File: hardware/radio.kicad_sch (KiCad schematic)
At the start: 22 parts, among them J9 Counterpoise, U6 Si4463

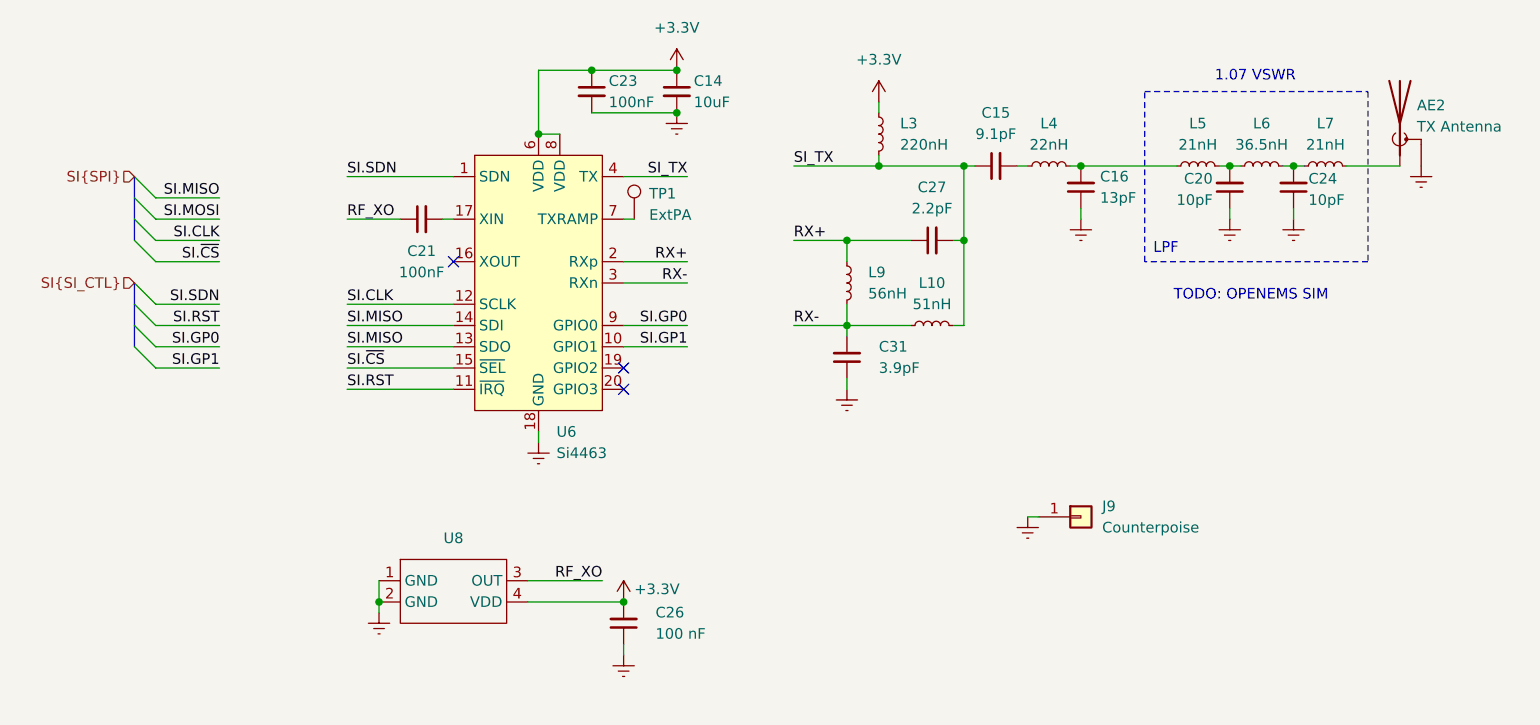
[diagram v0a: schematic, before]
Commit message: power path and bme280 fix
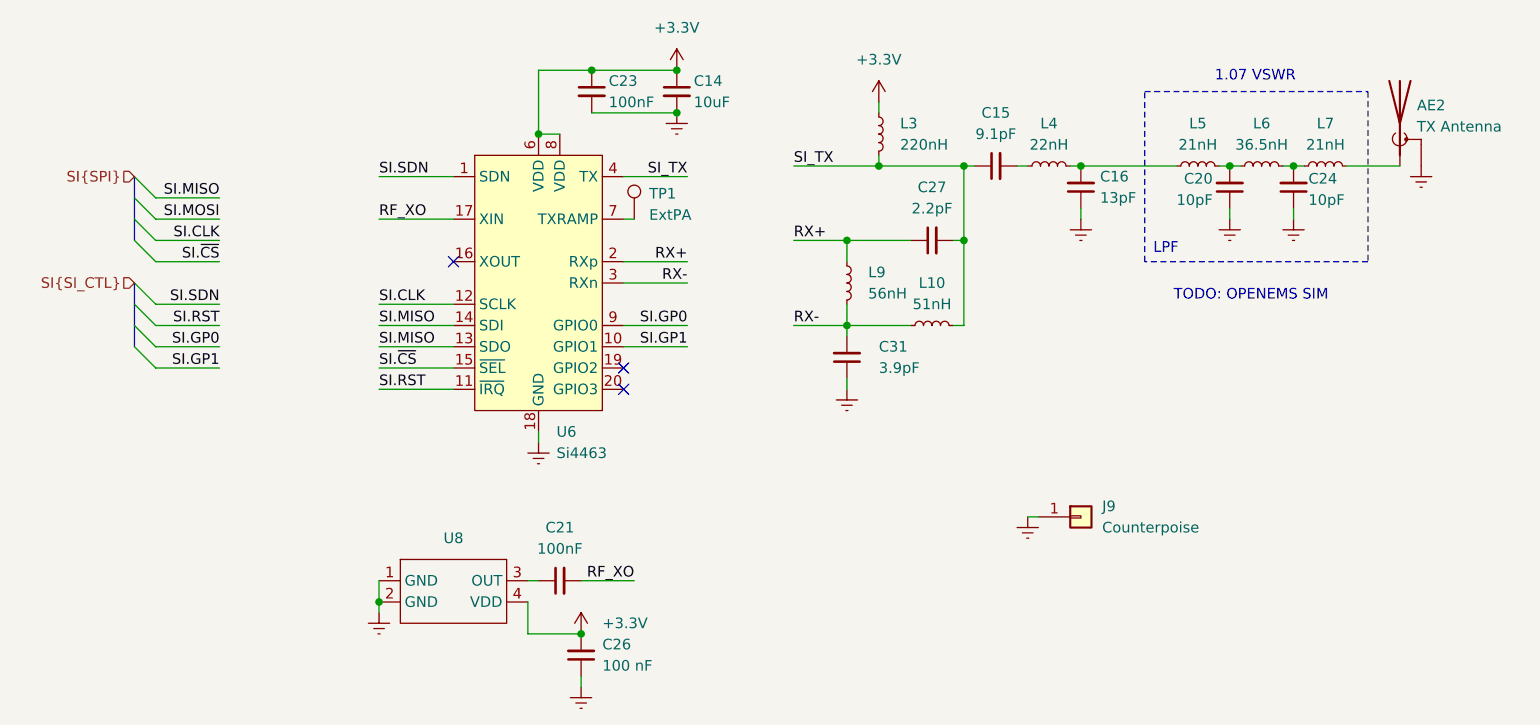
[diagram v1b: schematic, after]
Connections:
- net RF_XO: now also C21.2, U6.17 (XIN); no longer C21.1, U8.3 (OUT)
- new net: C21.1, U8.3 (OUT)
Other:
- moved on the sheet: C26
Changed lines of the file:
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@@
 	)
 	(junction
-		(at 147.32 62.23)
+		(at 135.89 129.54)
 		(diameter 0)
 		(color 0 0 0 0)
 	)
 	(junction
-		(at 181.61 73.66)
+		(at 147.32 62.23)
 		(diameter 0)
 		(color 0 0 0 0)
 	)
 	(junction
-		(at 167.64 92.71)
+		(at 181.61 73.66)
 		(diameter 0)
 		(color 0 0 0 0)
 	)
 	(junction
-		(at 140.97 125.73)
+		(at 167.64 92.71)
 		(diameter 0)
 		(color 0 0 0 0)
@@
 	(wire
 		(pts
-			(xy 107.95 95.25) (xy 120.65 95.25)
+			(xy 111.76 95.25) (xy 120.65 95.25)
 		)
 		(stroke
@@
 	(wire
 		(pts
-			(xy 107.95 92.71) (xy 120.65 92.71)
+			(xy 111.76 92.71) (xy 120.65 92.71)
 		)
 		(stroke
@@
 	(wire
 		(pts
-			(xy 107.95 80.01) (xy 114.3 80.01)
+			(xy 111.76 80.01) (xy 120.65 80.01)
 		)
 		(stroke
@@
 	(wire
 		(pts
-			(xy 138.43 123.19) (xy 129.54 123.19)
+			(xy 129.54 129.54) (xy 135.89 129.54)
 		)
 		(stroke
@@
 	(wire
 		(pts
-			(xy 107.95 97.79) (xy 120.65 97.79)
+			(xy 111.76 97.79) (xy 120.65 97.79)
 		)
 		(stroke
@@
 	(wire
 		(pts
+			(xy 135.89 123.19) (xy 142.24 123.19)
+		)
+		(stroke
+			(width 0)
+			(type default)
+		)
+	)
+	(wire
+		(pts
 			(xy 85.09 85.09) (xy 92.71 85.09)
 		)
@@
 	(wire
 		(pts
-			(xy 107.95 90.17) (xy 120.65 90.17)
+			(xy 111.76 90.17) (xy 120.65 90.17)
 		)
 		(stroke
@@
 	(wire
 		(pts
-			(xy 107.95 74.93) (xy 120.65 74.93)
+			(xy 111.76 74.93) (xy 120.65 74.93)
 		)
 		(stroke
@@
 	(wire
 		(pts
-			(xy 171.45 73.66) (xy 171.45 72.39)
+			(xy 129.54 123.19) (xy 130.81 123.19)
 		)
 		(stroke
@@
 	(wire
 		(pts
-			(xy 130.81 69.85) (xy 133.35 69.85)
+			(xy 171.45 73.66) (xy 171.45 72.39)
 		)
 		(stroke
@@
 	(wire
 		(pts
-			(xy 107.95 100.33) (xy 120.65 100.33)
+			(xy 130.81 69.85) (xy 133.35 69.85)
 		)
 		(stroke
@@
 	(wire
 		(pts
-			(xy 85.09 82.55) (xy 92.71 82.55)
+			(xy 111.76 100.33) (xy 120.65 100.33)
 		)
 		(stroke
@@
 	(wire
 		(pts
-			(xy 119.38 80.01) (xy 120.65 80.01)
+			(xy 85.09 82.55) (xy 92.71 82.55)
 		)
 		(stroke
@@
 	(wire
 		(pts
-			(xy 140.97 132.08) (xy 140.97 130.81)
+			(xy 135.89 135.89) (xy 135.89 134.62)
 		)
 		(stroke
@@
 	(wire
 		(pts
-			(xy 181.61 82.55) (xy 180.34 82.55)
+			(xy 129.54 129.54) (xy 129.54 125.73)
 		)
 		(stroke
@@
 	(wire
 		(pts
-			(xy 195.58 73.66) (xy 194.31 73.66)
+			(xy 181.61 82.55) (xy 180.34 82.55)
 		)
 		(stroke
@@
 	(wire
 		(pts
-			(xy 129.54 125.73) (xy 140.97 125.73)
+			(xy 195.58 73.66) (xy 194.31 73.66)
 		)
 		(stroke
@@
 	)
 	(label "SI.RST"
-		(at 107.95 100.33 0)
+		(at 111.76 100.33 0)
 		(effects
 			(font
@@
 	)
 	(label "SI.CLK"
-		(at 107.95 90.17 0)
+		(at 111.76 90.17 0)
 		(effects
 			(font
@@
 	)
 	(label "SI.SDN"
-		(at 107.95 74.93 0)
+		(at 111.76 74.93 0)
 		(effects
 			(font
@@
 	)
 	(label "SI.MISO"
-		(at 107.95 92.71 0)
+		(at 111.76 92.71 0)
 		(effects
 			(font
@@
 	)
 	(label "SI.~{CS}"
-		(at 107.95 97.79 0)
+		(at 111.76 97.79 0)
 		(effects
 			(font
@@
 	)
 	(label "RF_XO"
-		(at 107.95 80.01 0)
+		(at 111.76 80.01 0)
 		(effects
 			(font
@@
 	)
 	(label "RF_XO"
-		(at 138.43 123.19 180)
+		(at 142.24 123.19 180)
 		(effects
 			(font
@@
 	)
 	(label "SI.MISO"
-		(at 107.95 95.25 0)
+		(at 111.76 95.25 0)
 		(effects
 			(font
@@
 	(symbol
 		(lib_id "Device:C_Small")
-		(at 116.84 80.01 90)
+		(at 133.35 123.19 90)
 		(mirror x)
 		(unit 1)
@@
 		(fields_autoplaced yes)
 		(property "Reference" "C21"
-			(at 116.8463 83.82 90)
+			(at 133.3563 116.84 90)
 			(show_name no)
 			(do_not_autoplace no)
@@
 		)
 		(property "Value" "100nF"
-			(at 116.8463 86.36 90)
+			(at 133.3563 119.38 90)
 			(show_name no)
 			(do_not_autoplace no)
@@
 		)
 		(property "Footprint" "Capacitor_SMD:C_0402_1005Metric"
-			(at 116.84 80.01 0)
+			(at 133.35 123.19 0)
 			(hide yes)
 			(show_name no)
@@
 		)
 		(property "Datasheet" ""
-			(at 116.84 80.01 0)
+			(at 133.35 123.19 0)
 			(hide yes)
 			(show_name no)
@@
 		)
 		(property "Description" "Unpolarized capacitor, small symbol"
-			(at 116.84 80.01 0)
+			(at 133.35 123.19 0)
 			(hide yes)
 			(show_name no)
@@
 	(symbol
 		(lib_id "Device:C_Small")
-		(at 140.97 128.27 180)
+		(at 135.89 132.08 180)
 		(unit 1)
 		(body_style 1)
@@
 		(fields_autoplaced yes)
 		(property "Reference" "C26"
-			(at 144.78 126.9935 0)
+			(at 138.43 130.8035 0)
 			(show_name no)
 			(do_not_autoplace no)
@@
 		)
 		(property "Value" "100 nF"
-			(at 144.78 129.5335 0)
+			(at 138.43 133.3435 0)
 			(show_name no)
 			(do_not_autoplace no)
@@
 		)
 		(property "Footprint" "Capacitor_SMD:C_0402_1005Metric_Pad0.74x0.62mm_HandSolder"
-			(at 140.97 128.27 0)
+			(at 135.89 132.08 0)
 			(hide yes)
 			(show_name no)
@@
 		)
 		(property "Datasheet" ""
-			(at 140.97 128.27 0)
+			(at 135.89 132.08 0)
 			(hide yes)
 			(show_name no)
@@
 		)
 		(property "Description" "Unpolarized capacitor, small symbol"
-			(at 140.97 128.27 0)
+			(at 135.89 132.08 0)
 			(hide yes)
 			(show_name no)
@@
 		)
 		(property "LCSC" "C1525"
-			(at 140.97 128.27 90)
+			(at 135.89 132.08 90)
 			(hide yes)
 			(show_name no)
@@
 		(lib_name "+3.3V_2")
 		(lib_id "power:+3.3V")
-		(at 140.97 125.73 0)
+		(at 135.89 129.54 0)
 		(unit 1)
 		(body_style 1)
@@
 		(in_pos_files yes)
 		(dnp no)
+		(fields_autoplaced yes)
 		(property "Reference" "#PWR062"
-			(at 140.97 129.54 0)
+			(at 135.89 133.35 0)
 			(hide yes)
 			(show_name no)
@@
 		)
 		(property "Value" "+3.3V"
-			(at 142.24 124.2059 0)
+			(at 138.43 128.2699 0)
 			(show_name no)
 			(do_not_autoplace no)
@@
 		)
 		(property "Footprint" ""
-			(at 140.97 125.73 0)
+			(at 135.89 129.54 0)
 			(hide yes)
 			(show_name no)
@@
 		)
 		(property "Datasheet" ""
-			(at 140.97 125.73 0)
+			(at 135.89 129.54 0)
 			(hide yes)
 			(show_name no)
@@
 		)
 		(property "Description" ""
-			(at 140.97 125.73 0)
+			(at 135.89 129.54 0)
 			(hide yes)
 			(show_name no)
@@
 		(lib_name "Earth_2")
 		(lib_id "power:Earth")
-		(at 140.97 132.08 0)
+		(at 135.89 135.89 0)
 		(unit 1)
 		(body_style 1)
@@
 		(fields_autoplaced yes)
 		(property "Reference" "#PWR067"
-			(at 140.97 138.43 0)
+			(at 135.89 142.24 0)
 			(hide yes)
 			(show_name no)
@@
 		)
 		(property "Value" "Earth"
-			(at 140.97 135.89 0)
+			(at 135.89 139.7 0)
 			(hide yes)
 			(show_name no)
@@
 		)
 		(property "Footprint" ""
-			(at 140.97 132.08 0)
+			(at 135.89 135.89 0)
 			(hide yes)
 			(show_name no)
@@
 		)
 		(property "Datasheet" ""
-			(at 140.97 132.08 0)
+			(at 135.89 135.89 0)
 			(hide yes)
 			(show_name no)
@@
 		)
 		(property "Description" ""
-			(at 140.97 132.08 0)
+			(at 135.89 135.89 0)
 			(hide yes)
 			(show_name no)

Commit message: pcb rework -- layout subsections and rough floorplanning
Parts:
- AE2: footprint Antenna:Antenna_Whip -> Connector_Coaxial:SMA_Samtec_SMA-J-P-H-ST-EM1_EdgeMount
- C14, C23: footprint Capacitor_SMD:C_0402_1005Metric_Pad0.74x0.62mm_HandSolder -> Capacitor_SMD:C_0402_1005Metric
- C26: value 100 nF -> 100nF; footprint Capacitor_SMD:C_0402_1005Metric_Pad0.74x0.62mm_HandSolder -> Capacitor_SMD:C_0402_1005Metric

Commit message: net class shenanigans
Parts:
- C14, C15, C16, C20, C21, C23, C24, C26, C27, C31, L10, L3, L4, L5, L6, L7, L9: KiLib_Generator (none) -> SMD_2terminal_chip_molded
- J9: KiLib_Generator (none) -> connector/pin_header_socket
- U6: KiLib_Generator (none) -> package/no_lead
- U8: KiLib_Generator (none) -> crystal_resonator_oscillator
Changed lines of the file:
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@@
 		)
 	)
-	(wire
-		(pts
-			(xy 207.01 73.66) (xy 195.58 73.66)
-		)
-		(stroke
-			(width 0)
-			(type default)
-		)
-	)
 	(bus
 		(pts
@@
 	(wire
 		(pts
+			(xy 195.58 73.66) (xy 207.01 73.66)
+		)
+		(stroke
+			(width 0)
+			(type default)
+		)
+	)
+	(wire
+		(pts
 			(xy 167.64 100.33) (xy 167.64 99.06)
 		)
@@
 		(polyline
 			(pts
-				(xy 248.92 104.14) (xy 248.92 57.15) (xy 157.48 57.15) (xy 157.48 104.14)
+				(xy 160.02 93.98) (xy 160.02 71.12) (xy 231.14 71.12) (xy 231.14 76.2) (xy 189.23 76.2) (xy 189.23 93.98)
 			)
 			(stroke
@@
 		(length 2.54)
 		(shape round)
-		(at 203.2 57.15 0)
+		(at 196.85 71.12 0)
 		(fields_autoplaced yes)
 		(effects
@@
 		)
 		(property "Netclass" "50R"
-			(at 203.8985 54.61 0)
+			(at 197.5485 68.58 0)
 			(show_name no)
 			(do_not_autoplace no)
@@
 		)
 		(property "Component Class" ""
-			(at -68.58 15.24 0)
+			(at -78.74 20.32 0)
 			(show_name no)
 			(do_not_autoplace no)
@@
 			)
 		)
+		(property "KiLib_Generator" "SMD_2terminal_chip_molded"
+			(at 224.79 73.66 0)
+			(hide yes)
+			(show_name no)
+			(do_not_autoplace no)
+			(effects
+				(font
+					(size 1.27 1.27)
+				)
+			)
+		)
 		(pin "2"
 		)
@@
 			)
 		)
+		(property "KiLib_Generator" "SMD_2terminal_chip_molded"
+			(at 133.35 123.19 0)
+			(hide yes)
+			(show_name no)
+			(do_not_autoplace no)
+			(effects
+				(font
+					(size 1.27 1.27)
+				)
+			)
+		)
 		(pin "2"
 		)
@@
 			)
 		)
+		(property "KiLib_Generator" "SMD_2terminal_chip_molded"
+			(at 195.58 76.2 0)
+			(hide yes)
+			(show_name no)
+			(do_not_autoplace no)
+			(effects
+				(font
+					(size 1.27 1.27)
+				)
+			)
+		)
 		(pin "2"
 		)
@@
 			)
 		)
+		(property "KiLib_Generator" "SMD_2terminal_chip_molded"
+			(at 213.36 76.2 0)
+			(hide yes)
+			(show_name no)
+			(do_not_autoplace no)
+			(effects
+				(font
+					(size 1.27 1.27)
+				)
+			)
+		)
 		(pin "2"
 		)
@@
 			)
 		)
+		(property "KiLib_Generator" "SMD_2terminal_chip_molded"
+			(at 135.89 132.08 0)
+			(hide yes)
+			(show_name no)
+			(do_not_autoplace no)
+			(effects
+				(font
+					(size 1.27 1.27)
+				)
+			)
+		)
 		(pin "1"
 		)
@@
 			)
 		)
+		(property "KiLib_Generator" "SMD_2terminal_chip_molded"
+			(at 137.16 64.77 0)
+			(hide yes)
+			(show_name no)
+			(do_not_autoplace no)
+			(effects
+				(font
+					(size 1.27 1.27)
+				)
+			)
+		)
 		(pin "1"
 		)
@@
 			)
 		)
+		(property "KiLib_Generator" "SMD_2terminal_chip_molded"
+			(at 171.45 69.85 0)
+			(hide yes)
+			(show_name no)
+			(do_not_autoplace no)
+			(effects
+				(font
+					(size 1.27 1.27)
+				)
+			)
+		)
 		(pin "2"
 		)
@@
 			)
 		)
+		(property "KiLib_Generator" "package/no_lead"
+			(at 130.81 87.63 0)
+			(hide yes)
+			(show_name no)
+			(do_not_autoplace no)
+			(effects
+				(font
+					(size 1.27 1.27)
+				)
+			)
+		)
 		(pin "21"
 		)
@@
 			)
 		)
+		(property "KiLib_Generator" "SMD_2terminal_chip_molded"
+			(at 177.8 92.71 0)
+			(hide yes)
+			(show_name no)
+			(do_not_autoplace no)
+			(effects
+				(font
+					(size 1.27 1.27)
+				)
+			)
+		)
 		(pin "2"
 		)
@@
 			)
 		)
+		(property "KiLib_Generator" "SMD_2terminal_chip_molded"
+			(at 191.77 73.66 0)
+			(hide yes)
+			(show_name no)
+			(do_not_autoplace no)
+			(effects
+				(font
+					(size 1.27 1.27)
+				)
+			)
+		)
 		(pin "2"
 		)
@@
 			)
 		)
+		(property "KiLib_Generator" "SMD_2terminal_chip_molded"
+			(at 167.64 87.63 0)
+			(hide yes)
+			(show_name no)
+			(do_not_autoplace no)
+			(effects
+				(font
+					(size 1.27 1.27)
+				)
+			)
+		)
 		(pin "2"
 		)
@@
 			)
 		)
+		(property "KiLib_Generator" "SMD_2terminal_chip_molded"
+			(at 167.64 96.52 0)
+			(hide yes)
+			(show_name no)
+			(do_not_autoplace no)
+			(effects
+				(font
+					(size 1.27 1.27)
+				)
+			)
+		)
 		(pin "2"
 		)
@@
 			)
 		)
+		(property "KiLib_Generator" "SMD_2terminal_chip_molded"
+			(at 177.8 82.55 0)
+			(hide yes)
+			(show_name no)
+			(do_not_autoplace no)
+			(effects
+				(font
+					(size 1.27 1.27)
+				)
+			)
+		)
 		(pin "2"
 		)
@@
 			)
 		)
+		(property "KiLib_Generator" "SMD_2terminal_chip_molded"
+			(at 220.98 76.2 0)
+			(hide yes)
+			(show_name no)
+			(do_not_autoplace no)
+			(effects
+				(font
+					(size 1.27 1.27)
+				)
+			)
+		)
 		(pin "2"
 		)
@@
 			)
 		)
+		(property "KiLib_Generator" "connector/pin_header_socket"
+			(at 195.58 115.57 0)
+			(hide yes)
+			(show_name no)
+			(do_not_autoplace no)
+			(effects
+				(font
+					(size 1.27 1.27)
+				)
+			)
+		)
 		(pin "1"
 		)
@@
 			)
 		)
+		(property "KiLib_Generator" "SMD_2terminal_chip_molded"
+			(at 217.17 73.66 0)
+			(hide yes)
+			(show_name no)
+			(do_not_autoplace no)
+			(effects
+				(font
+					(size 1.27 1.27)
+				)
+			)
+		)
 		(pin "2"
 		)
@@
 			)
 		)
+		(property "KiLib_Generator" "SMD_2terminal_chip_molded"
+			(at 185.42 73.66 0)
+			(hide yes)
+			(show_name no)
+			(do_not_autoplace no)
+			(effects
+				(font
+					(size 1.27 1.27)
+				)
+			)
+		)
 		(pin "2"
 		)
@@
 			)
 		)
+		(property "KiLib_Generator" "SMD_2terminal_chip_molded"
+			(at 209.55 73.66 0)
+			(hide yes)
+			(show_name no)
+			(do_not_autoplace no)
+			(effects
+				(font
+					(size 1.27 1.27)
+				)
+			)
+		)
 		(pin "2"
 		)
@@
 			)
 		)
+		(property "KiLib_Generator" "SMD_2terminal_chip_molded"
+			(at 147.32 64.77 0)
+			(hide yes)
+			(show_name no)
+			(do_not_autoplace no)
+			(effects
+				(font
+					(size 1.27 1.27)
+				)
+			)
+		)
 		(pin "1"
 		)
@@
 			(at 120.65 120.65 0)
 			(hide yes)
+			(show_name no)
+			(do_not_autoplace no)
+			(effects
+				(font
+					(size 1.27 1.27)
+				)
+			)
+		)
+		(property "KiLib_Generator" "crystal_resonator_oscillator"
+			(at 120.65 120.65 0)
+			(hide yes)

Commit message: draft of routing
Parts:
- removed J9: Counterpoise, Connector_PinHeader_2.54mm:PinHeader_1x01_P2.54mm_Vertical, symbol Connector_Generic:Conn_01x01
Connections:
- net SI.MISO: no longer U6.14 (SDI)
- net SI.MOSI: now also U6.14 (SDI)
- net SI_TX: no longer C27.2, L10.2
- net at C16.2, L4.2, L5.1: now also C27.2, L10.2
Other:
- moved on the sheet: C15, L4
